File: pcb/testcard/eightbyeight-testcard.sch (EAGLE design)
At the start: 28 parts

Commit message: Update test card with proper sized holes
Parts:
- +3V3, ESP_GPIO16, ESP_GPIO5, GND: value TEST_POINT -> TEST_POINT2.55MM; device DevicesToMerge:TEST_POINT -> DevicesToMerge:TEST_POINT2.55MM
- 5V, ARM_3V3, ARM_BOOT, ARM_RESET, ARM_RX, ARM_RX1, ARM_TCK, ARM_TMS, ARM_TX, BOOST_5V, BUTTON, ESP_GPIO0, ESP_RESET, GND_, I2C_SCL, I2C_SDA, LED_CLK, LED_DATA, LED_OE, LED_STB, VBAT: value TEST_POINT -> TEST_POINT1.4MM; device DevicesToMerge:TEST_POINT -> DevicesToMerge:TEST_POINT1.4MM
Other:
- note added: "Revision Notes/Changelog Revision A: -Matches Rev D/E/F application versions Revision B: -Put connectors and labels on proper side -Make test card longer to give space for ribbon cables"
- note removed: "Revision Notes/Changelog Revision A: Matches Rev D/E/F application versions"
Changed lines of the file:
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@@
 </variantdefs>
 <classes>
-<class number="0" name="default" width="0" drill="0">
+<class number="0" name="default" width="0.4064" drill="0.35">
 </class>
-<class number="1" name="power" width="0.254" drill="0.35">
+<class number="1" name="power" width="0.4064" drill="0.35">
 </class>
 </classes>
@@
 <part name="FRAME2" library="frames" deviceset="A3L-LOC" device=""/>
 <part name="FRAME6" library="frames" deviceset="A3P-LOC" device=""/>
-<part name="ARM_BOOT" library="DevicesToMerge" deviceset="TEST_POINT" device=""/>
+<part name="ARM_BOOT" library="DevicesToMerge" deviceset="TEST_POINT" device="1.4MM" value="TEST_POINT1.4MM"/>
 <part name="3V7" library="supply1" deviceset="+3V3" device=""/>
 <part name="GND44" library="supply1" deviceset="GND" device=""/>
-<part name="LED_DATA" library="DevicesToMerge" deviceset="TEST_POINT" device=""/>
-<part name="LED_CLK" library="DevicesToMerge" deviceset="TEST_POINT" device=""/>
-<part name="LED_STB" library="DevicesToMerge" deviceset="TEST_POINT" device=""/>
-<part name="LED_OE" library="DevicesToMerge" deviceset="TEST_POINT" device=""/>
-<part name="I2C_SDA" library="DevicesToMerge" deviceset="TEST_POINT" device=""/>
-<part name="I2C_SCL" library="DevicesToMerge" deviceset="TEST_POINT" device=""/>
-<part name="5V" library="DevicesToMerge" deviceset="TEST_POINT" device=""/>
-<part name="VBAT" library="DevicesToMerge" deviceset="TEST_POINT" device=""/>
+<part name="LED_DATA" library="DevicesToMerge" deviceset="TEST_POINT" device="1.4MM" value="TEST_POINT1.4MM"/>
+<part name="LED_CLK" library="DevicesToMerge" deviceset="TEST_POINT" device="1.4MM" value="TEST_POINT1.4MM"/>
+<part name="LED_STB" library="DevicesToMerge" deviceset="TEST_POINT" device="1.4MM" value="TEST_POINT1.4MM"/>
+<part name="LED_OE" library="DevicesToMerge" deviceset="TEST_POINT" device="1.4MM" value="TEST_POINT1.4MM"/>
+<part name="I2C_SDA" library="DevicesToMerge" deviceset="TEST_POINT" device="1.4MM" value="TEST_POINT1.4MM"/>
+<part name="I2C_SCL" library="DevicesToMerge" deviceset="TEST_POINT" device="1.4MM" value="TEST_POINT1.4MM"/>
+<part name="5V" library="DevicesToMerge" deviceset="TEST_POINT" device="1.4MM" value="TEST_POINT1.4MM"/>
+<part name="VBAT" library="DevicesToMerge" deviceset="TEST_POINT" device="1.4MM" value="TEST_POINT1.4MM"/>
 <part name="P+6" library="supply1" deviceset="+5V" device=""/>
-<part name="ARM_3V3" library="DevicesToMerge" deviceset="TEST_POINT" device=""/>
-<part name="ARM_TMS" library="DevicesToMerge" deviceset="TEST_POINT" device=""/>
-<part name="ARM_TCK" library="DevicesToMerge" deviceset="TEST_POINT" device=""/>
-<part name="ARM_TX" library="DevicesToMerge" deviceset="TEST_POINT" device=""/>
-<part name="ARM_RX" library="DevicesToMerge" deviceset="TEST_POINT" device=""/>
-<part name="ARM_RESET" library="DevicesToMerge" deviceset="TEST_POINT" device=""/>
-<part name="ESP_GPIO0" library="DevicesToMerge" deviceset="TEST_POINT" device=""/>
-<part name="ESP_RESET" library="DevicesToMerge" deviceset="TEST_POINT" device=""/>
-<part name="GND_" library="DevicesToMerge" deviceset="TEST_POINT" device=""/>
+<part name="ARM_3V3" library="DevicesToMerge" deviceset="TEST_POINT" device="1.4MM" value="TEST_POINT1.4MM"/>
+<part name="ARM_TMS" library="DevicesToMerge" deviceset="TEST_POINT" device="1.4MM" value="TEST_POINT1.4MM"/>
+<part name="ARM_TCK" library="DevicesToMerge" deviceset="TEST_POINT" device="1.4MM" value="TEST_POINT1.4MM"/>
+<part name="ARM_TX" library="DevicesToMerge" deviceset="TEST_POINT" device="1.4MM" value="TEST_POINT1.4MM"/>
+<part name="ARM_RX" library="DevicesToMerge" deviceset="TEST_POINT" device="1.4MM" value="TEST_POINT1.4MM"/>
+<part name="ARM_RESET" library="DevicesToMerge" deviceset="TEST_POINT" device="1.4MM" value="TEST_POINT1.4MM"/>
+<part name="ESP_GPIO0" library="DevicesToMerge" deviceset="TEST_POINT" device="1.4MM" value="TEST_POINT1.4MM"/>
+<part name="ESP_RESET" library="DevicesToMerge" deviceset="TEST_POINT" device="1.4MM" value="TEST_POINT1.4MM"/>
+<part name="GND_" library="DevicesToMerge" deviceset="TEST_POINT" device="1.4MM" value="TEST_POINT1.4MM"/>
 <part name="GND22" library="supply1" deviceset="GND" device=""/>
-<part name="ARM_RX1" library="DevicesToMerge" deviceset="TEST_POINT" device=""/>
-<part name="BOOST_5V" library="DevicesToMerge" deviceset="TEST_POINT" device=""/>
-<part name="BUTTON" library="DevicesToMerge" deviceset="TEST_POINT" device=""/>
-<part name="GND" library="DevicesToMerge" deviceset="TEST_POINT" device=""/>
-<part name="ESP_GPIO5" library="DevicesToMerge" deviceset="TEST_POINT" device=""/>
-<part name="ESP_GPIO16" library="DevicesToMerge" deviceset="TEST_POINT" device=""/>
-<part name="+3V3" library="DevicesToMerge" deviceset="TEST_POINT" device=""/>
+<part name="ARM_RX1" library="DevicesToMerge" deviceset="TEST_POINT" device="1.4MM" value="TEST_POINT1.4MM"/>
+<part name="BOOST_5V" library="DevicesToMerge" deviceset="TEST_POINT" device="1.4MM" value="TEST_POINT1.4MM"/>
+<part name="BUTTON" library="DevicesToMerge" deviceset="TEST_POINT" device="1.4MM" value="TEST_POINT1.4MM"/>
+<part name="GND" library="DevicesToMerge" deviceset="TEST_POINT" device="2.55MM"/>
+<part name="ESP_GPIO5" library="DevicesToMerge" deviceset="TEST_POINT" device="2.55MM"/>
+<part name="ESP_GPIO16" library="DevicesToMerge" deviceset="TEST_POINT" device="2.55MM"/>
+<part name="+3V3" library="DevicesToMerge" deviceset="TEST_POINT" device="2.55MM"/>
 <part name="JTAG" library="blinkinlabs" deviceset="JTAG_ARM_10PIN" device=""/>
 <part name="GND1" library="supply1" deviceset="GND" device=""/>
@@
 <text x="17.78" y="325.12" size="3.81" layer="91" align="top-left">Revision Notes/Changelog
 Revision A:
-Matches Rev D/E/F application versions</text>
+-Matches Rev D/E/F application versions
+Revision B:
+-Put connectors and labels on proper side
+-Make test card longer to give space for ribbon cables</text>
 <text x="129.54" y="358.14" size="10.16" layer="91" align="bottom-center">EightByEight Test card</text>
 <text x="129.54" y="345.44" size="6.4516" layer="91" align="bottom-center">Copyright 2016 Blinkinlabs, LLC</text>

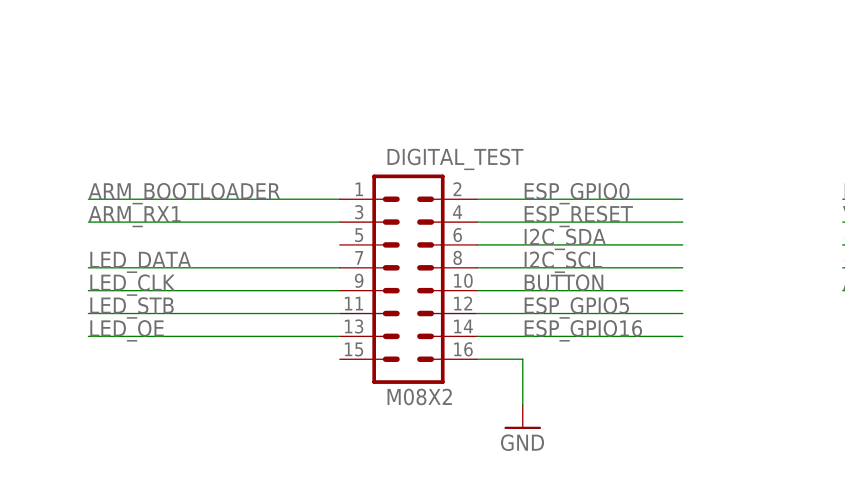
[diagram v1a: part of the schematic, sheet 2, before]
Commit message: Update testcard to fit current test jig
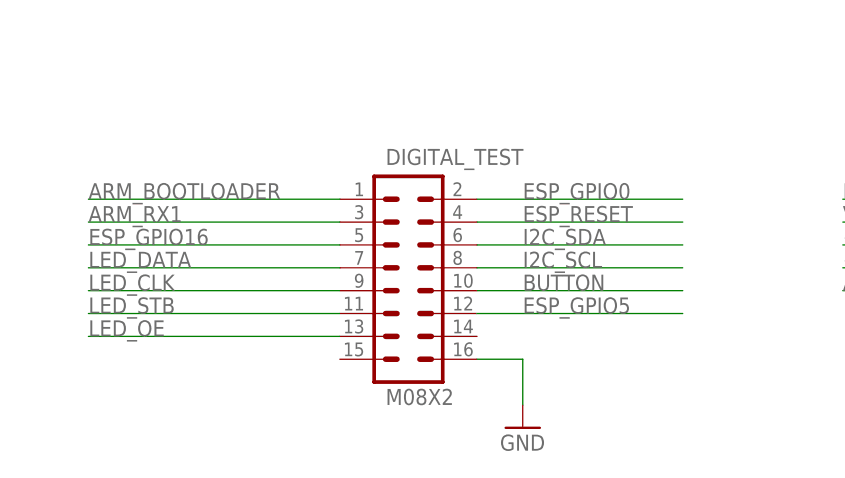
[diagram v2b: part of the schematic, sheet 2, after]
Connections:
- net ESP_GPIO16: now also DIGITAL_TEST.5; no longer DIGITAL_TEST.14
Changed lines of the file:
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@@
 <?xml version="1.0" encoding="utf-8"?>
 <!DOCTYPE eagle SYSTEM "eagle.dtd">
-<eagle version="7.6.0">
+<eagle version="7.5.0">
 <drawing>
 <settings>
@@
 </segment>
 <segment>
-<pinref part="DIGITAL_TEST" gate="G$1" pin="14"/>
-<wire x1="58.42" y1="35.56" x2="81.28" y2="35.56" width="0.1524" layer="91"/>
-<label x="63.5" y="35.56" size="1.778" layer="95"/>
-</segment>
-</net>
+<pinref part="DIGITAL_TEST" gate="G$1" pin="5"/>
+<wire x1="43.18" y1="45.72" x2="15.24" y2="45.72" width="0.1524" layer="91"/>
+<label x="15.24" y="45.72" size="1.778" layer="95"/>
+</segment>
+</net>

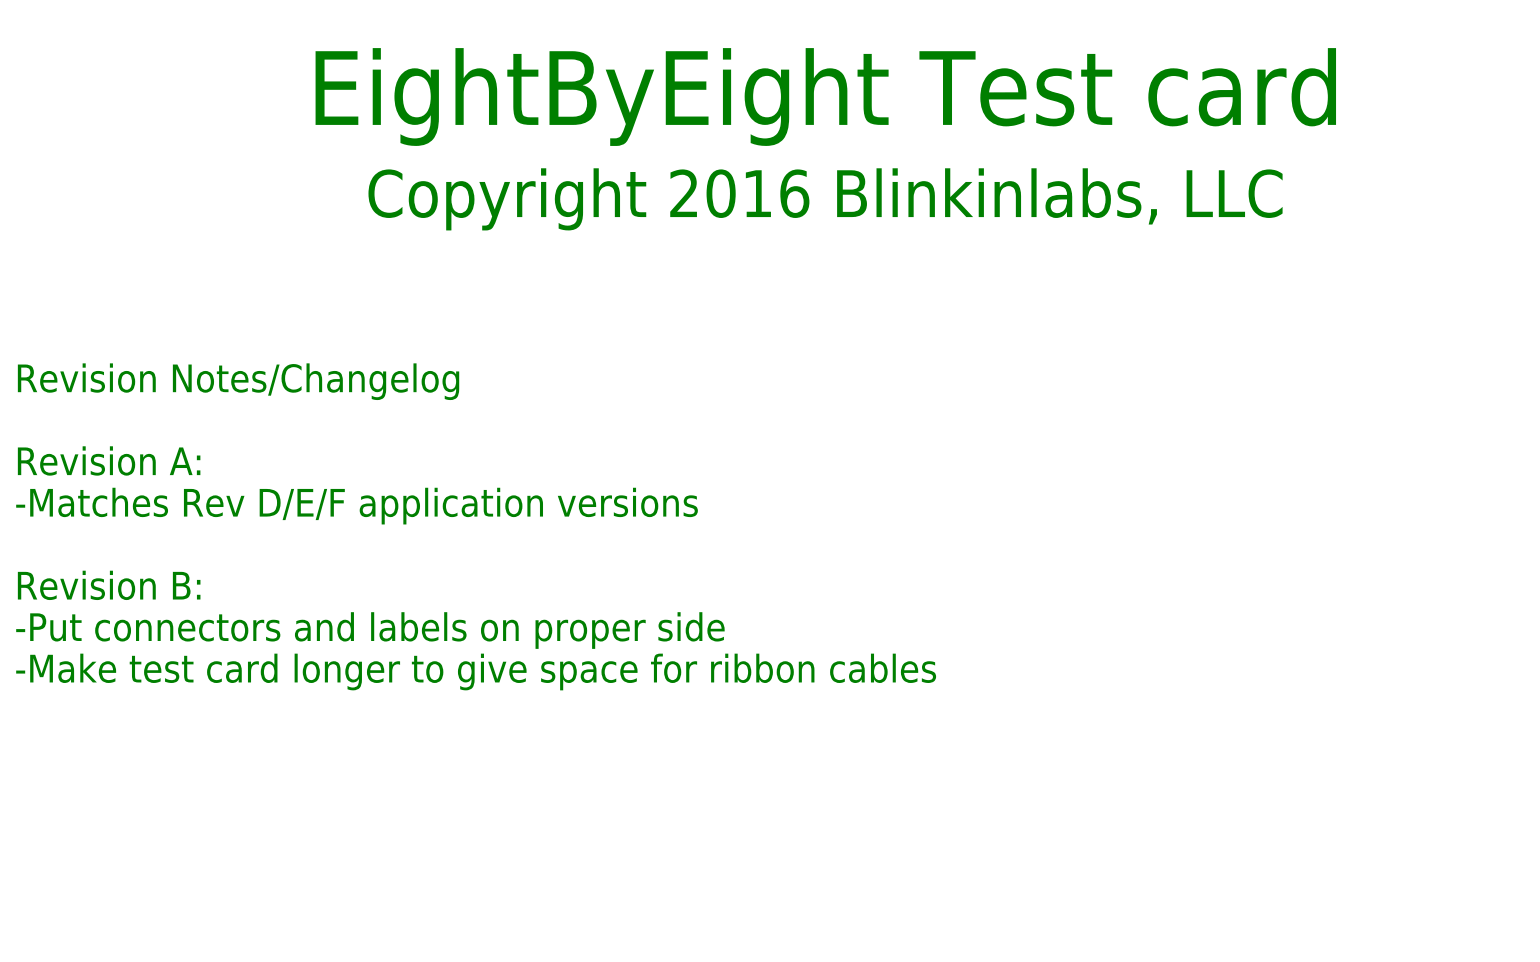
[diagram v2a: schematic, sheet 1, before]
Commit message: Update test card pcb notes
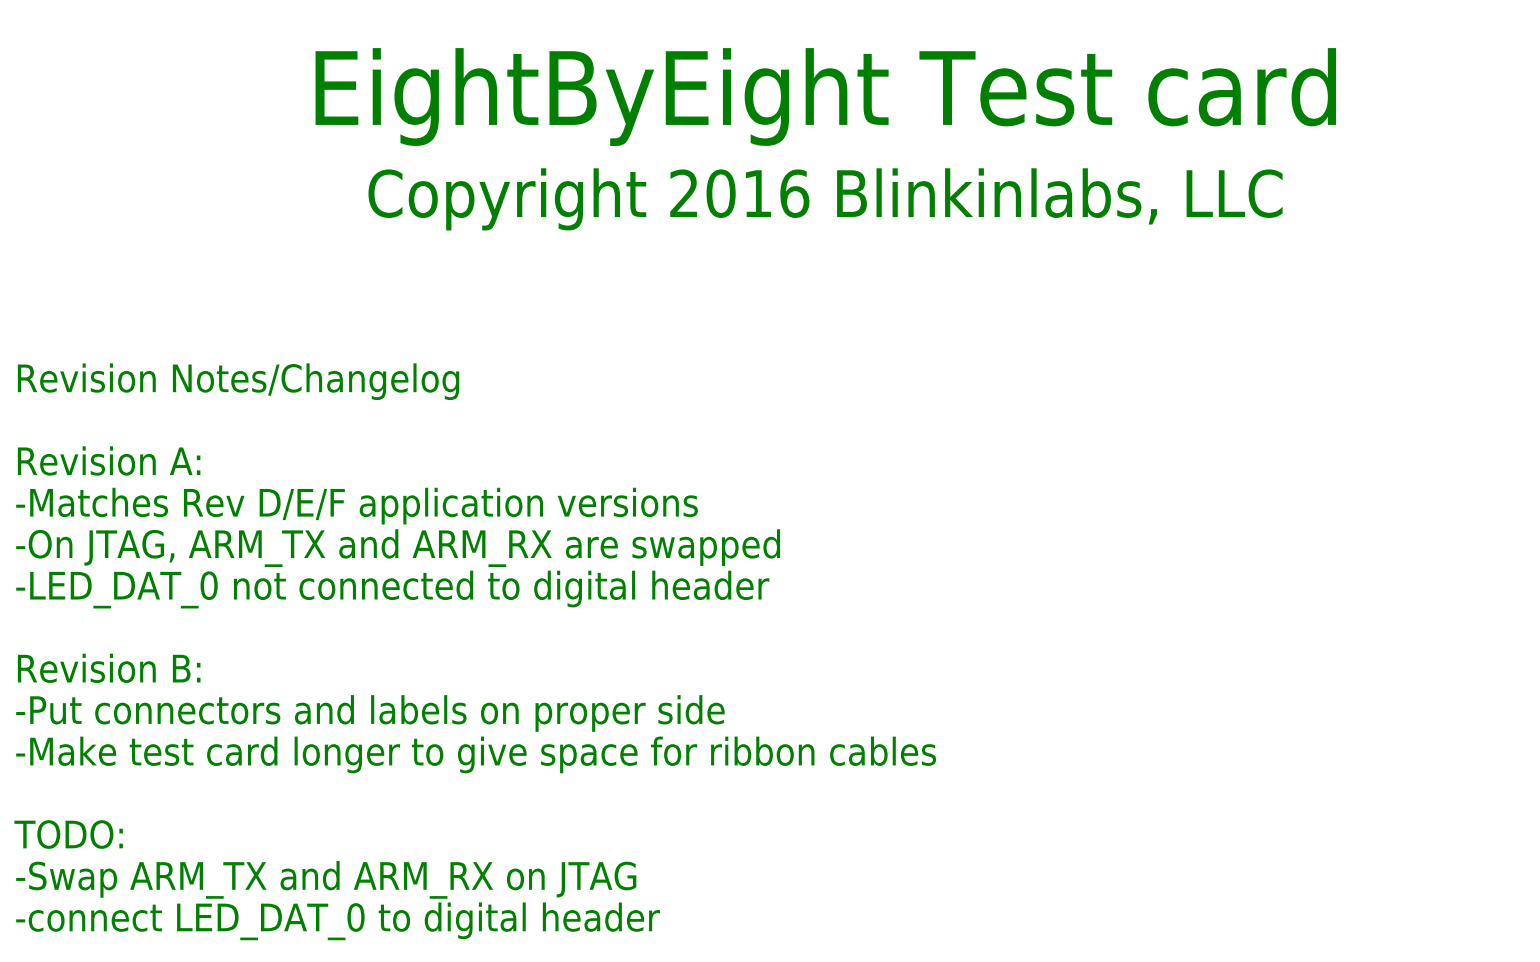
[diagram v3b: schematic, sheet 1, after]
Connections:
- removed net LED_DATA: DIGITAL_TEST.7
- net LED_DAT_0: now also DIGITAL_TEST.7
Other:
- note added: "Revision Notes/Changelog Revision A: -Matches Rev D/E/F application versions -On JTAG, ARM_TX and ARM_RX are swapped -LED_DAT_0 not connected to digital header Revision B: -Put connectors and labels on proper side -Make test card longer to give space for ribbon cables TODO: -Swap ARM_TX and ARM_RX on JTAG -connect LED_DAT_0 to digital header"
- note removed: "Revision Notes/Changelog Revision A: -Matches Rev D/E/F application versions Revision B: -Put connectors and labels on proper side -Make test card longer to give space for ribbon cables"
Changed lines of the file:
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@@
 Revision A:
 -Matches Rev D/E/F application versions
+-On JTAG, ARM_TX and ARM_RX are swapped
+-LED_DAT_0 not connected to digital header
 Revision B:
 -Put connectors and labels on proper side
--Make test card longer to give space for ribbon cables</text>
+-Make test card longer to give space for ribbon cables
+TODO:
+-Swap ARM_TX and ARM_RX on JTAG
+-connect LED_DAT_0 to digital header</text>
 <text x="129.54" y="358.14" size="10.16" layer="91" align="bottom-center">EightByEight Test card</text>
 <text x="129.54" y="345.44" size="6.4516" layer="91" align="bottom-center">Copyright 2016 Blinkinlabs, LLC</text>
@@
 <label x="182.88" y="144.78" size="1.778" layer="95"/>
 </segment>
+<segment>
+<pinref part="DIGITAL_TEST" gate="G$1" pin="7"/>
+<wire x1="43.18" y1="43.18" x2="15.24" y2="43.18" width="0.1524" layer="91"/>
+<label x="15.24" y="43.18" size="1.778" layer="95"/>
+</segment>
 </net>
 <net name="LED_OE" class="0">
@@
 </segment>
 </net>
-<net name="LED_DATA" class="0">
-<segment>
-<pinref part="DIGITAL_TEST" gate="G$1" pin="7"/>
-<wire x1="43.18" y1="43.18" x2="15.24" y2="43.18" width="0.1524" layer="91"/>
-<label x="15.24" y="43.18" size="1.778" layer="95"/>
-</segment>
-</net>
 <net name="ESP_GPIO5" class="0">
 <segment>
@@
 </sheet>
 </sheets>
-<errors>
-</errors>
 </schematic>
 </drawing>
